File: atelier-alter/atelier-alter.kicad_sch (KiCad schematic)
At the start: 55 parts, among them SW1 SW_DPST, SW2 SW_DPST, SW3 SW_DPST, SW4 RESET, U1 ATmega32U4-A, U2 PRTR5V0U2X, Y1 16Mhz

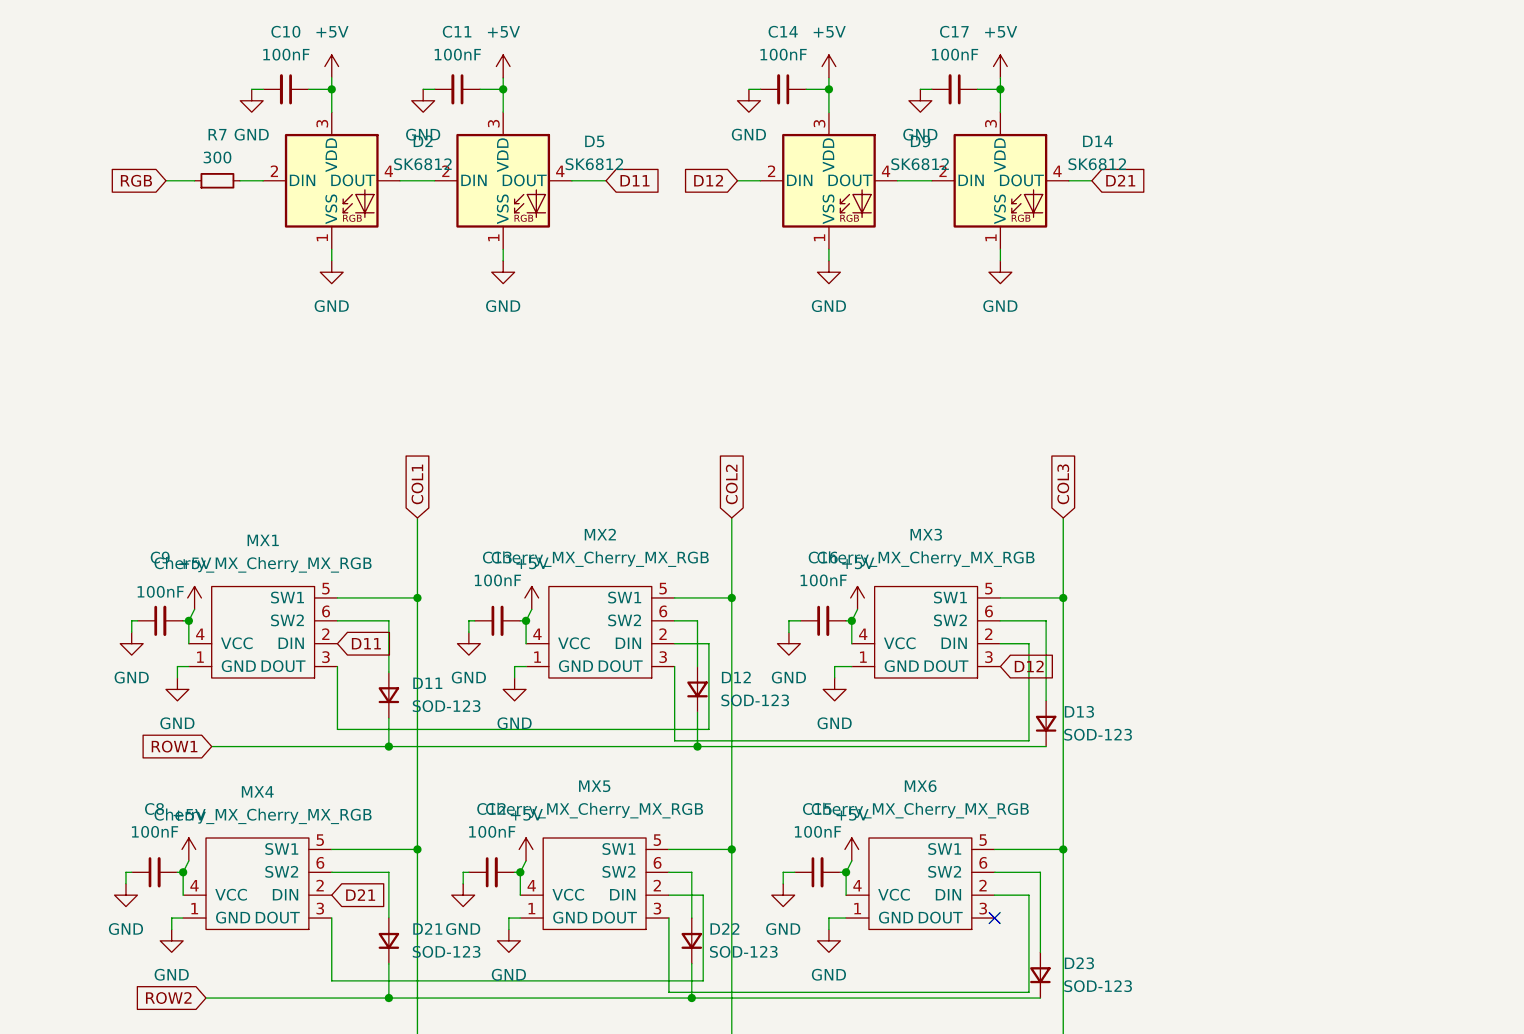
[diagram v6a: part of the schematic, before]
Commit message: small tweaks, done drawing the case
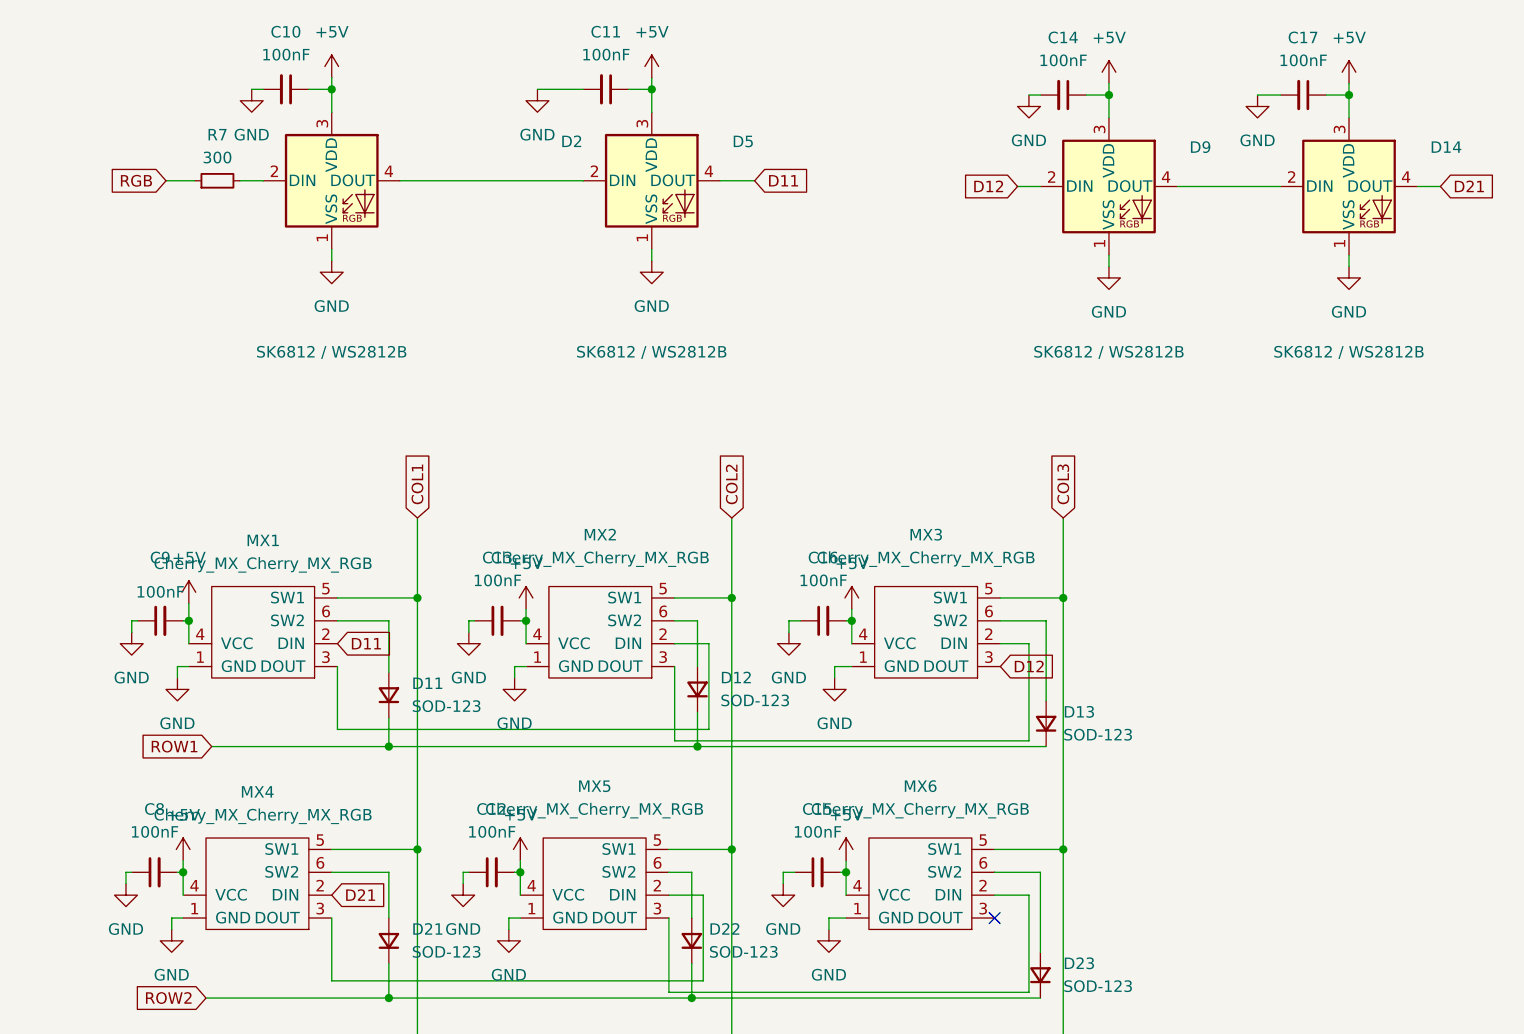
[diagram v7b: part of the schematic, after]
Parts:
- D14, D2, D5, D9: value SK6812 -> SK6812 / WS2812B; footprint LED_SMD:LED_SK6812_PLCC4_5.0x5.0mm_P3.2mm -> LED_SMD:LED_WS2812B_PLCC4_5.0x5.0mm_P3.2mm
- H1, H2, H3, H4: footprint MountingHole:MountingHole_2.5mm -> MountingHole:MountingHole_2.2mm_M2
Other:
- moved on the sheet: C11, C14, C17, D14, D5, D9

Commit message: minor updates here and there
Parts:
- H1, H2, H3, H4: footprint MountingHole:MountingHole_2.2mm_M2 -> MountingHole:MountingHole_5.3mm_M5
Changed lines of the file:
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@@
       (effects (font (size 1.27 1.27)) (justify left))
     )
-    (property "Footprint" "MountingHole:MountingHole_2.2mm_M2" (id 2) (at 129.54 186.69 0)
+    (property "Footprint" "MountingHole:MountingHole_5.3mm_M5" (id 2) (at 129.54 186.69 0)
       (effects (font (size 1.27 1.27)) hide)
     )
@@
       (effects (font (size 1.27 1.27)) (justify left))
     )
-    (property "Footprint" "MountingHole:MountingHole_2.2mm_M2" (id 2) (at 106.68 186.69 0)
+    (property "Footprint" "MountingHole:MountingHole_5.3mm_M5" (id 2) (at 106.68 186.69 0)
       (effects (font (size 1.27 1.27)) hide)
     )
@@
       (effects (font (size 1.27 1.27)) (justify left))
     )
-    (property "Footprint" "MountingHole:MountingHole_2.2mm_M2" (id 2) (at 106.68 176.53 0)
+    (property "Footprint" "MountingHole:MountingHole_5.3mm_M5" (id 2) (at 106.68 176.53 0)
       (effects (font (size 1.27 1.27)) hide)
     )
@@
       (effects (font (size 1.27 1.27)) (justify left))
     )
-    (property "Footprint" "MountingHole:MountingHole_2.2mm_M2" (id 2) (at 129.54 176.53 0)
+    (property "Footprint" "MountingHole:MountingHole_5.3mm_M5" (id 2) (at 129.54 176.53 0)
       (effects (font (size 1.27 1.27)) hide)
     )
@@
     )
     (path "/8556b1bc-59f1-44d9-99ff-e1f2c0ffcf36"
-      (reference "H1") (unit 1) (value "MountingHole") (footprint "MountingHole:MountingHole_2.2mm_M2")
+      (reference "H1") (unit 1) (value "MountingHole") (footprint "MountingHole:MountingHole_5.3mm_M5")
     )
     (path "/5a99e80a-11b8-48d3-b554-660c0bcf5c38"
-      (reference "H2") (unit 1) (value "MountingHole") (footprint "MountingHole:MountingHole_2.2mm_M2")
+      (reference "H2") (unit 1) (value "MountingHole") (footprint "MountingHole:MountingHole_5.3mm_M5")
     )
     (path "/9a99f614-4356-46fa-a338-e647cb700704"
-      (reference "H3") (unit 1) (value "MountingHole") (footprint "MountingHole:MountingHole_2.2mm_M2")
+      (reference "H3") (unit 1) (value "MountingHole") (footprint "MountingHole:MountingHole_5.3mm_M5")
     )
     (path "/3b67de7c-1c99-408a-a31c-508b13725aa4"
-      (reference "H4") (unit 1) (value "MountingHole") (footprint "MountingHole:MountingHole_2.2mm_M2")
+      (reference "H4") (unit 1) (value "MountingHole") (footprint "MountingHole:MountingHole_5.3mm_M5")
     )
     (path "/92fbf038-747f-4dcc-ac4a-6dcc9e81a6d6"
